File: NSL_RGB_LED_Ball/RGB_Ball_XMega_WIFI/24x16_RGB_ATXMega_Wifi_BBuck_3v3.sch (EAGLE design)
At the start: 118 parts, among them IC2 TLC5947XLP, IC3 TLC5947XLP, IC4 TLC5947XLP, IC5 MCP73123, IC6 CC3000, IC7 MMA7455L, IC8 OPA344, IC9 TPS6300X, X1 NX3225GA-16.000M-STD-CRG-2

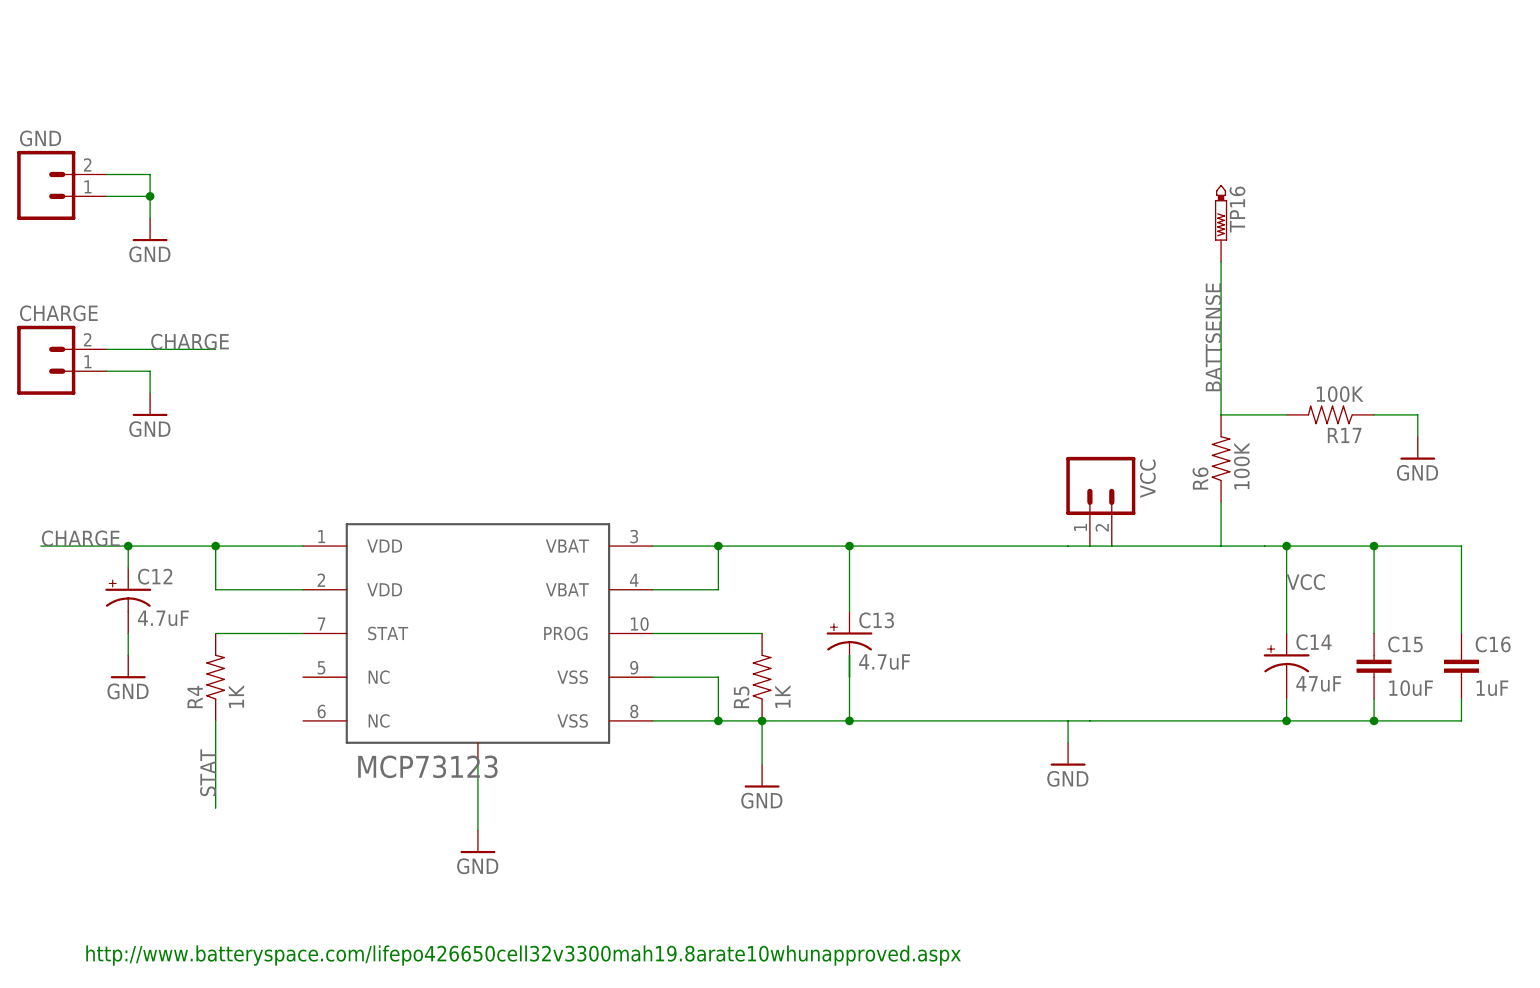
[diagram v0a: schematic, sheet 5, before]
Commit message: 
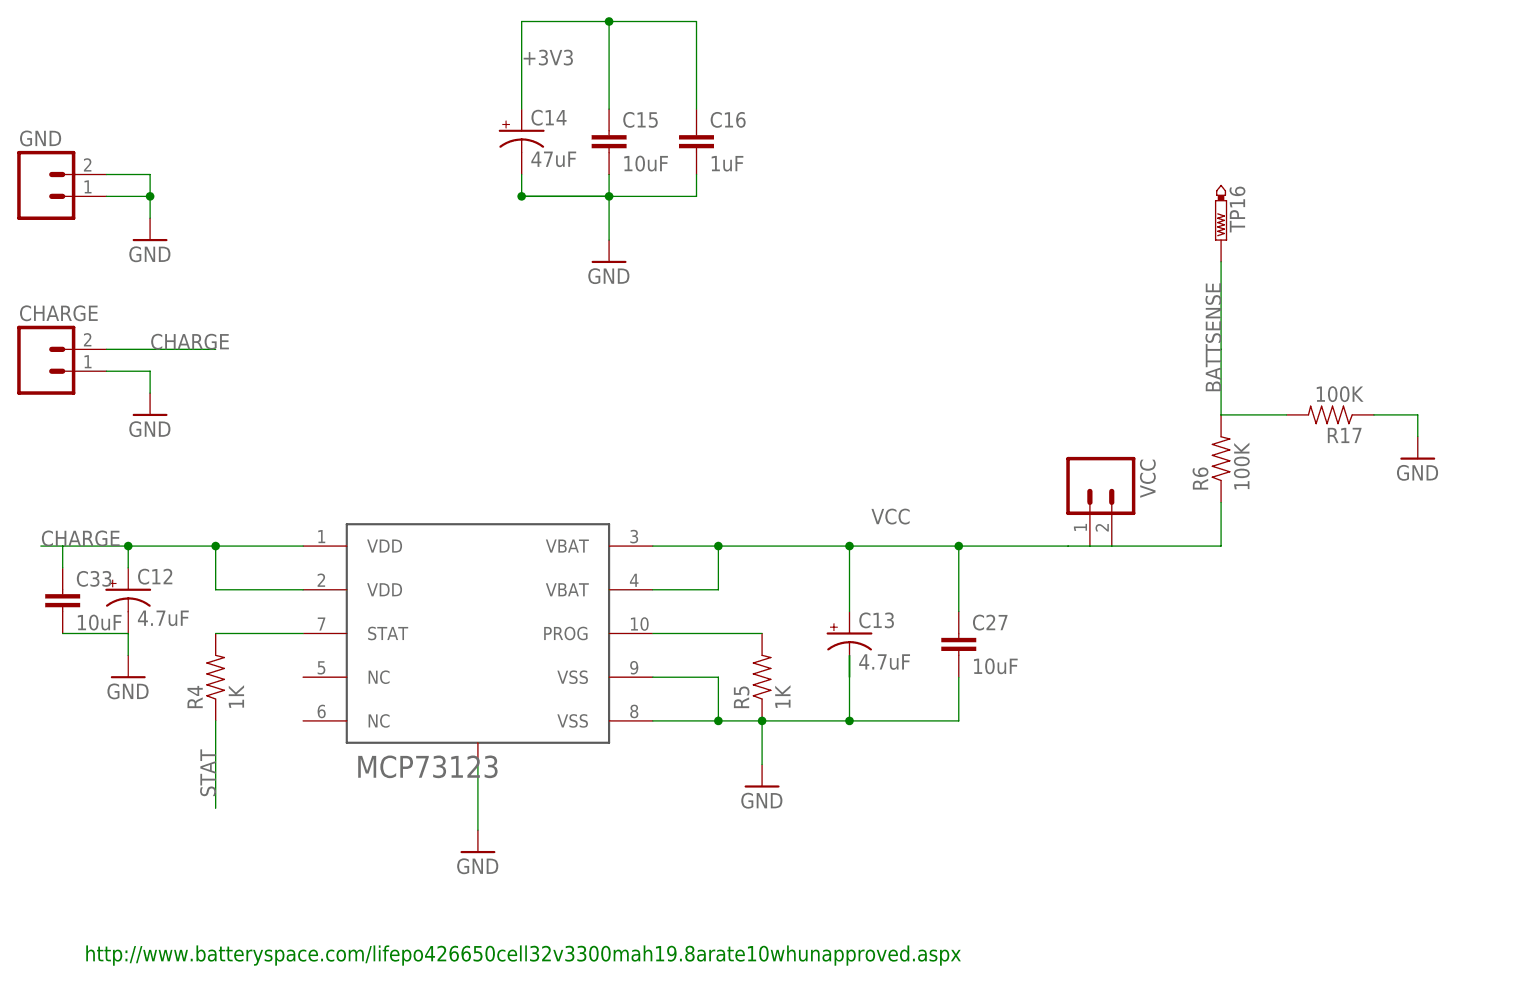
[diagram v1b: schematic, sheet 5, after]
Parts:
- added C27, C33: 10uF, 24x16_RGB:CAP0805
- added R7: 100K, CH_passive:RESISTOR0805
- added R9: 340K, CH_passive:RESISTOR0805
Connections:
- new net VINA: IC9.VINA, R7.1, R9.1
- net +3V3: now also C10.1, C11.1, C14.+, C15.1, C16.1, C19.2, C9.1, IC2.VCC, IC3.VCC, IC4.VCC, IC6.VBAT_IN, LED1.A, LED10.A, LED11.A, LED12.A, LED13.A, LED14.A, LED15.A, LED16.A, LED17.A, LED18.A, LED19.A, LED2.A, LED20.A, LED21.A, LED22.A, LED23.A, LED24.A, LED3.A, LED4.A, LED5.A, LED6.A, LED7.A, LED8.A, LED9.A
- net CHARGE: now also C33.1
- net GND: now also C27.2, C33.2, R9.2
- net N$32: no longer IC9.VINA
- net VCC: now also C27.1, R7.2; no longer C10.1, C11.1, C14.+, C15.1, C16.1, C19.2, C9.1, IC2.VCC, IC3.VCC, IC4.VCC, IC6.VBAT_IN, LED1.A, LED10.A, LED11.A, LED12.A, LED13.A, LED14.A, LED15.A, LED16.A, LED17.A, LED18.A, LED19.A, LED2.A, LED20.A, LED21.A, LED22.A, LED23.A, LED24.A, LED3.A, LED4.A, LED5.A, LED6.A, LED7.A, LED8.A, LED9.A
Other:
- moved on the sheet: C14, C15, C16
